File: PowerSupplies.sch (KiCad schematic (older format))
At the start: 37 parts, among them Q301 BC847B-13-F, Q302 BC856B-13-F, Q305 TK32A12N1,S4X, Q306 TK32A12N1,S4X, U301 FDA217, U302 LTC7138EMSE-PBF, U303 TPS560200, U304 TLV70430_SOT23-5

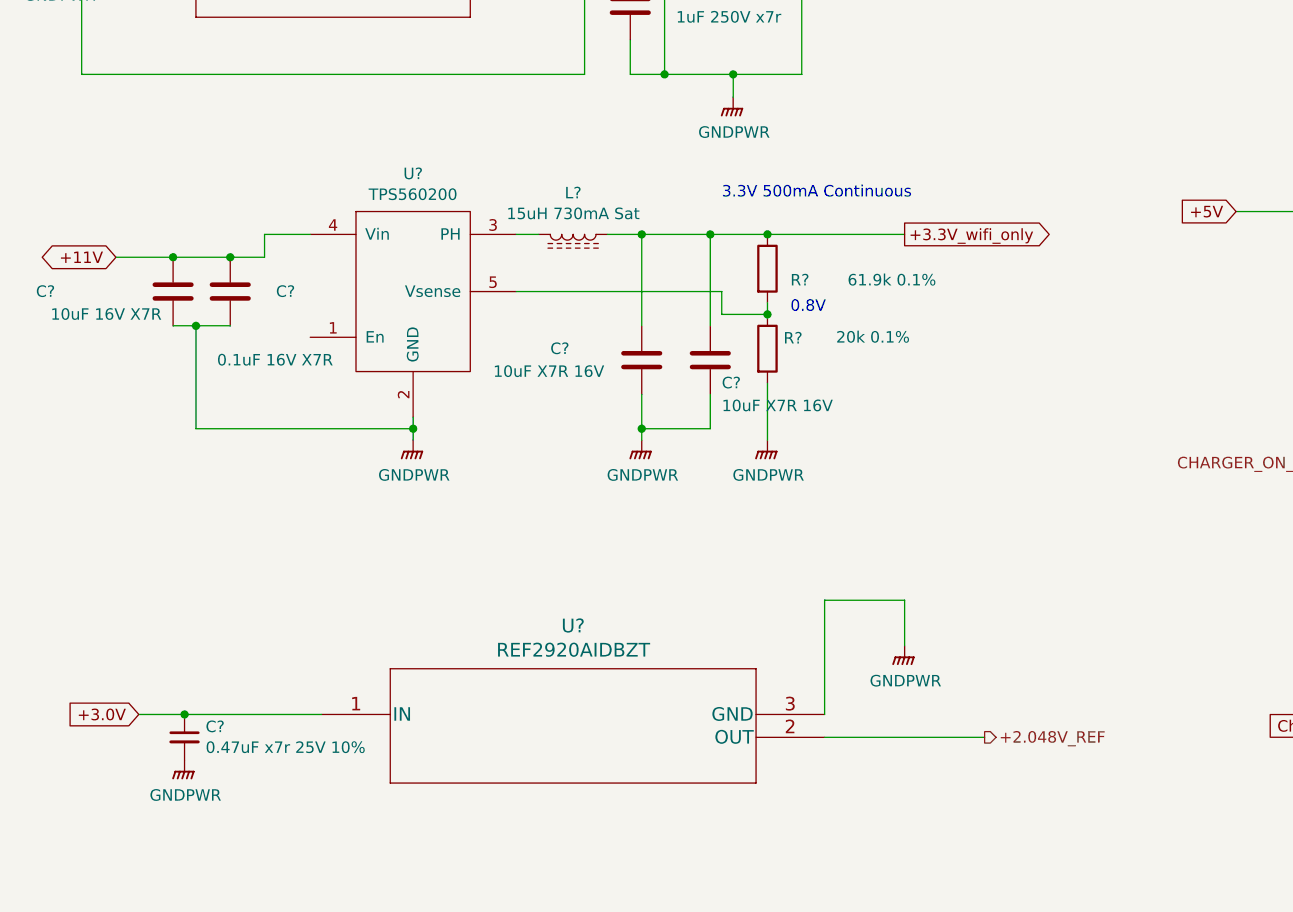
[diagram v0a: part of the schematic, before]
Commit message: started routing backing up tonnes of changes,2.048V reference changed to 2.5V ref, to match ucc2800, cos to change to a version with a 2V feedback, would require me to update the Oscillator cap and resistor,and also recalulate the class 2 loop compensation components etc.  Move the location of the teensy LC and added the ESP-WROOM-o2 wifi module.
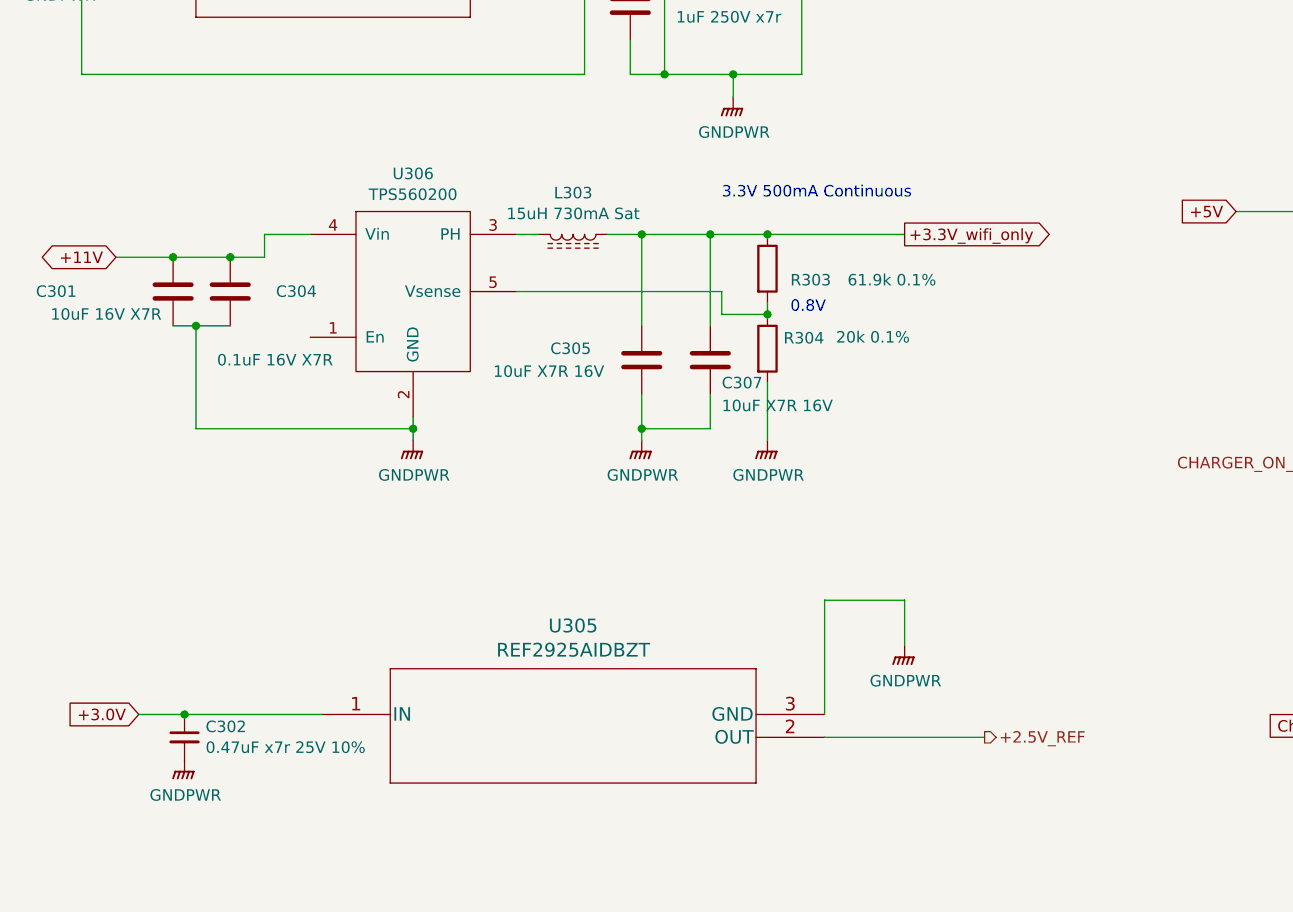
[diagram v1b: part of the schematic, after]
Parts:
- U305: renamed from U?; value REF2920AIDBZT -> REF2925AIDBZT
- gave numbers to parts that had none: 9
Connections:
- net +2.048V_REF renamed +2.5V_REF
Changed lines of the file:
@@
 5V 500mA Continuous
 Text HLabel 4750 5900 2    50   Output ~ 0
-+2.048V_REF
++2.5V_REF
 Text GLabel 950  3800 0    50   BiDi ~ 0
 +11V
@@
 P 2250 4600
 AR Path="/5F9C831E" Ref="#PWR?"  Part="1"
-AR Path="/5EBD6442/5F9C831E" Ref="#PWR?"  Part="1"
-F 0 "#PWR?" H 2250 4400 50  0001 C CNN
+AR Path="/5EBD6442/5F9C831E" Ref="#PWR0303"  Part="1"
+F 0 "#PWR0303" H 2250 4400 50  0001 C CNN
 F 1 "GNDPWR" H 2254 4446 50  0000 C CNN
 F 2 "" H 2250 4550 50  0001 C CNN
@@
 P 3550 4250
 AR Path="/5F9C8324" Ref="C?"  Part="1"
-AR Path="/5EBD6442/5F9C8324" Ref="C?"  Part="1"
-F 0 "C?" H 3600 4150 50  0000 L CNN
+AR Path="/5EBD6442/5F9C8324" Ref="C307"  Part="1"
+F 0 "C307" H 3600 4150 50  0000 L CNN
 F 1 "10uF X7R 16V" H 3600 4050 50  0000 L CNN
 F 2 "Capacitors_SMD:C_1206_HandSoldering" H 3588 4100 50  0001 C CNN
@@
 P 2950 3700
 AR Path="/5F9C832A" Ref="L?"  Part="1"
-AR Path="/5EBD6442/5F9C832A" Ref="L?"  Part="1"
-F 0 "L?" V 2769 3700 50  0000 C CNN
+AR Path="/5EBD6442/5F9C832A" Ref="L303"  Part="1"
+F 0 "L303" V 2769 3700 50  0000 C CNN
 F 1 "15uH 730mA Sat" V 2860 3700 50  0000 C CNN
 F 2 "Inductors_jl:Inductor_1210_HandSoldering" H 2950 3700 50  0001 C CNN
@@
 P 3250 4250
 AR Path="/5F9C8331" Ref="C?"  Part="1"
-AR Path="/5EBD6442/5F9C8331" Ref="C?"  Part="1"
-F 0 "C?" H 2850 4300 50  0000 L CNN
+AR Path="/5EBD6442/5F9C8331" Ref="C305"  Part="1"
+F 0 "C305" H 2850 4300 50  0000 L CNN
 F 1 "10uF X7R 16V" H 2600 4200 50  0000 L CNN
 F 2 "Capacitors_SMD:C_1206_HandSoldering" H 3288 4100 50  0001 C CNN
@@
 P 3800 3850
 AR Path="/5F9C8337" Ref="R?"  Part="1"
-AR Path="/5EBD6442/5F9C8337" Ref="R?"  Part="1"
-F 0 "R?" H 3900 3800 50  0000 L CNN
+AR Path="/5EBD6442/5F9C8337" Ref="R303"  Part="1"
+F 0 "R303" H 3900 3800 50  0000 L CNN
 F 1 "61.9k 0.1%" H 4150 3800 50  0000 L CNN
 F 2 "Resistors_SMD:R_0805_HandSoldering" V 3730 3850 50  0001 C CNN
@@
 P 3800 4200
 AR Path="/5F9C833D" Ref="R?"  Part="1"
-AR Path="/5EBD6442/5F9C833D" Ref="R?"  Part="1"
-F 0 "R?" H 3870 4246 50  0000 L CNN
+AR Path="/5EBD6442/5F9C833D" Ref="R304"  Part="1"
+F 0 "R304" H 3870 4246 50  0000 L CNN
 F 1 "20k 0.1%" H 4100 4250 50  0000 L CNN
 F 2 "Resistors_SMD:R_0805_HandSoldering" V 3730 4200 50  0001 C CNN
@@
 P 3800 4600
 AR Path="/5F9C8343" Ref="#PWR?"  Part="1"
-AR Path="/5EBD6442/5F9C8343" Ref="#PWR?"  Part="1"
-F 0 "#PWR?" H 3800 4400 50  0001 C CNN
+AR Path="/5EBD6442/5F9C8343" Ref="#PWR0305"  Part="1"
+F 0 "#PWR0305" H 3800 4400 50  0001 C CNN
 F 1 "GNDPWR" H 3804 4446 50  0000 C CNN
 F 2 "" H 3800 4550 50  0001 C CNN
@@
 P 3250 4600
 AR Path="/5F9C834D" Ref="#PWR?"  Part="1"
-AR Path="/5EBD6442/5F9C834D" Ref="#PWR?"  Part="1"
-F 0 "#PWR?" H 3250 4400 50  0001 C CNN
+AR Path="/5EBD6442/5F9C834D" Ref="#PWR0304"  Part="1"
+F 0 "#PWR0304" H 3250 4400 50  0001 C CNN
 F 1 "GNDPWR" H 3254 4446 50  0000 C CNN
 F 2 "" H 3250 4550 50  0001 C CNN
@@
 P 1200 3950
 AR Path="/5F9C8354" Ref="C?"  Part="1"
-AR Path="/5EBD6442/5F9C8354" Ref="C?"  Part="1"
-F 0 "C?" H 600 3950 50  0000 L CNN
+AR Path="/5EBD6442/5F9C8354" Ref="C301"  Part="1"
+F 0 "C301" H 600 3950 50  0000 L CNN
 F 1 "10uF 16V X7R" H 1150 3850 50  0000 R CNN
 F 2 "Capacitors_SMD:C_1206_HandSoldering" H 1238 3800 50  0001 C CNN
@@
 0.8V
 $Comp
-L TI:TPS560200 U?
+L TI:TPS560200 U306
 U 1 1 5F9C8360
 P 2250 3950
-F 0 "U?" H 2250 4465 50  0000 C CNN
+F 0 "U306" H 2250 4465 50  0000 C CNN
 F 1 "TPS560200" H 2250 4374 50  0000 C CNN
 F 2 "Package_TO_SOT_SMD:SOT-23-5_HandSoldering" H 2250 3950 50  0001 C CNN
@@
 P 1450 3950
 AR Path="/5F9C836F" Ref="C?"  Part="1"
-AR Path="/5EBD6442/5F9C836F" Ref="C?"  Part="1"
-F 0 "C?" H 1650 3950 50  0000 L CNN
+AR Path="/5EBD6442/5F9C836F" Ref="C304"  Part="1"
+F 0 "C304" H 1650 3950 50  0000 L CNN
 F 1 "0.1uF 16V X7R" H 1900 3650 50  0000 R CNN
 F 2 "Capacitors_SMD:C_0805_HandSoldering" H 1488 3800 50  0001 C CNN
@@
 3.3V 500mA Continuous
 $Comp
-L TI:REF2920AIDBZT U?
+L TI:REF2920AIDBZT U305
 U 1 1 5FB58010
 P 1850 5800
-F 0 "U?" H 2950 6187 60  0000 C CNN
-F 1 "REF2920AIDBZT" H 2950 6081 60  0000 C CNN
+F 0 "U305" H 2950 6187 60  0000 C CNN
+F 1 "REF2925AIDBZT" H 2950 6081 60  0000 C CNN
 F 2 "Package_TO_SOT_SMD:SOT-23_Handsoldering" H 2950 6040 60  0001 C CNN
 F 3 "" H 1850 5800 60  0000 C CNN
@@
 P 4400 5500
 AR Path="/5FB595B9" Ref="#PWR?"  Part="1"
-AR Path="/5EBD6442/5FB595B9" Ref="#PWR?"  Part="1"
-F 0 "#PWR?" H 4400 5300 50  0001 C CNN
+AR Path="/5EBD6442/5FB595B9" Ref="#PWR0306"  Part="1"
+F 0 "#PWR0306" H 4400 5300 50  0001 C CNN
 F 1 "GNDPWR" H 4404 5346 50  0000 C CNN
 F 2 "" H 4400 5450 50  0001 C CNN
@@
 	4050 5900 4750 5900
 $Comp
-L Device:C_Small C?
+L Device:C_Small C302
 U 1 1 5FB88319
 P 1250 5900
-F 0 "C?" H 1342 5946 50  0000 L CNN
+F 0 "C302" H 1342 5946 50  0000 L CNN
 F 1 "0.47uF x7r 25V 10%" H 1342 5855 50  0000 L CNN
 F 2 "Capacitors_SMD:C_0805_HandSoldering" H 1250 5900 50  0001 C CNN
@@
 P 1250 6000
 AR Path="/5FB8F7FD" Ref="#PWR?"  Part="1"
-AR Path="/5EBD6442/5FB8F7FD" Ref="#PWR?"  Part="1"
-F 0 "#PWR?" H 1250 5800 50  0001 C CNN
+AR Path="/5EBD6442/5FB8F7FD" Ref="#PWR0302"  Part="1"
+F 0 "#PWR0302" H 1250 5800 50  0001 C CNN
 F 1 "GNDPWR" H 1254 5846 50  0000 C CNN
 F 2 "" H 1250 5950 50  0001 C CNN

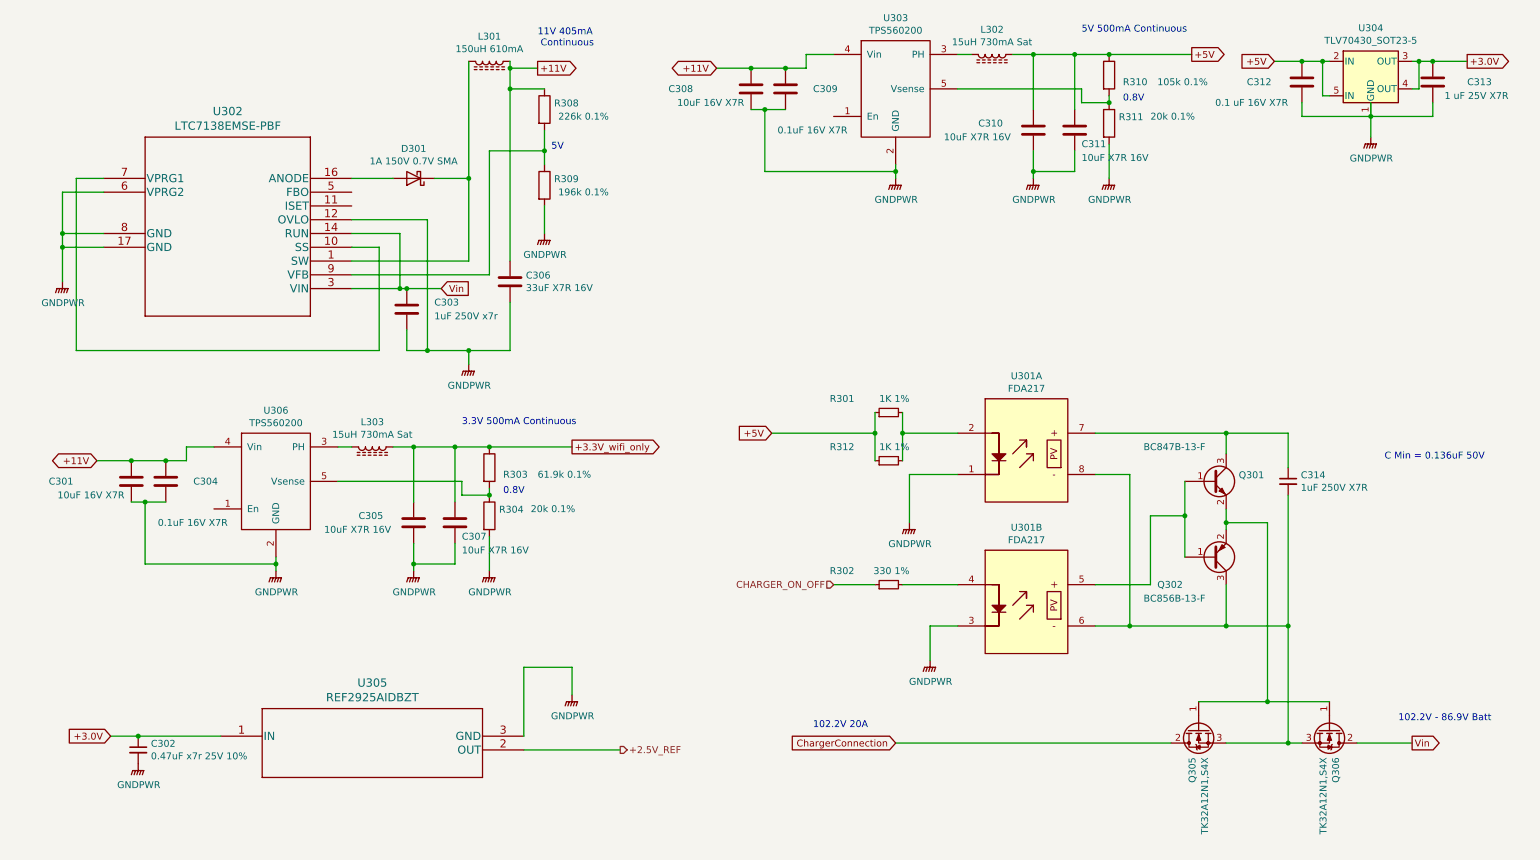
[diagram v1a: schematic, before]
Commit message: added testpoints
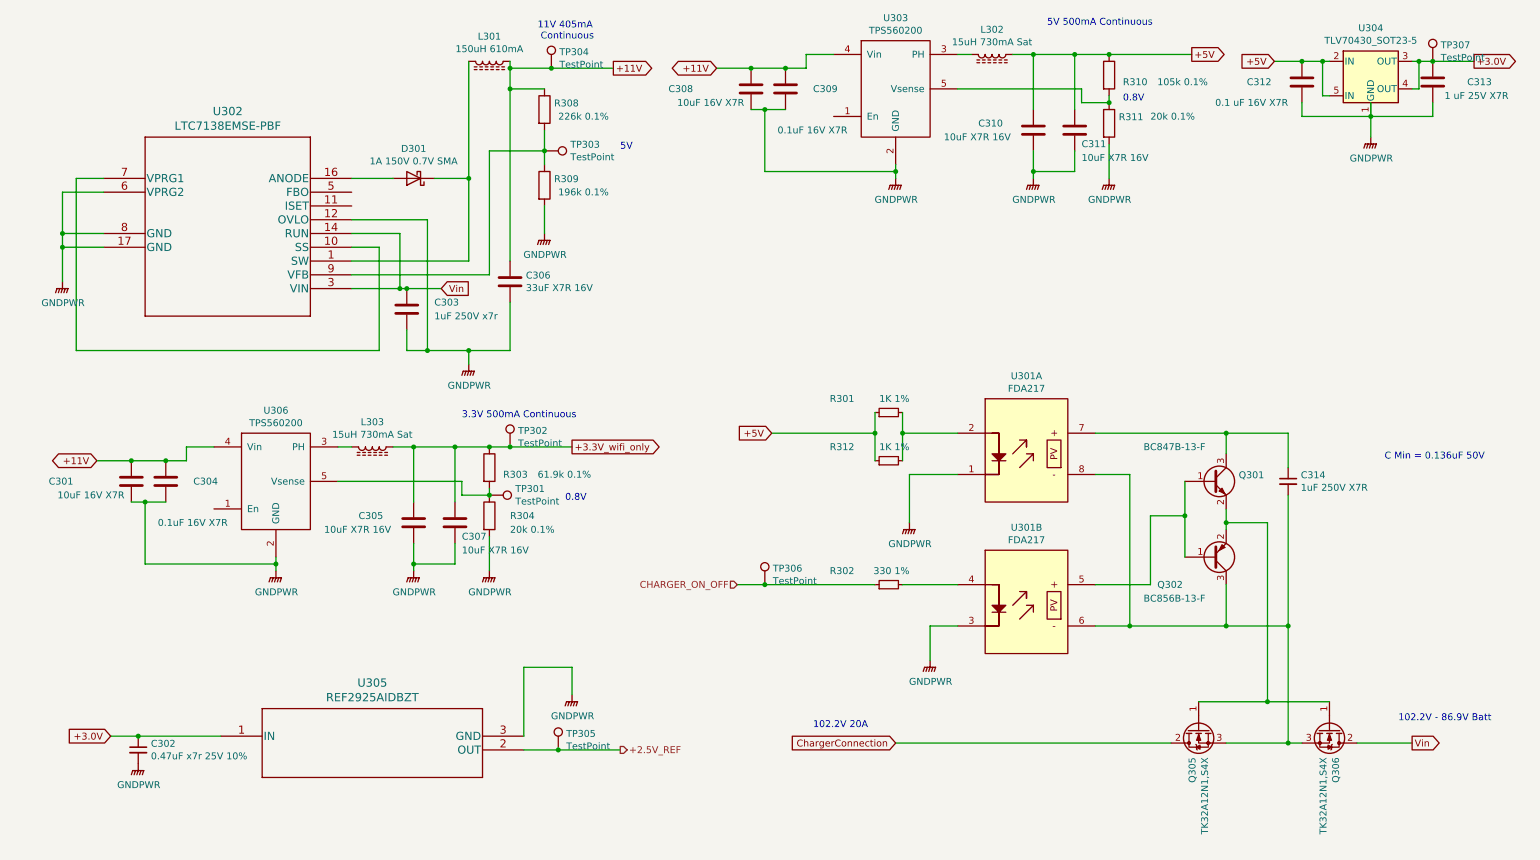
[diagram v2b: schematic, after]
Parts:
- added TP301, TP302, TP303, TP304, TP305, TP306, TP307: TestPoint, Measurement_Points:Measurement_Point_Square-SMD-Pad_Big, symbol Connector:TestPoint
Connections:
- net +11V: now also TP304.1
- net +2.5V_REF: now also TP305.1
- net +3.0V: now also TP307.1
- net +3.3V_wifi_only: now also TP302.1
- net CHARGER_ON_OFF: now also TP306.1
- net at R308.2, R309.1, U302.9 (VFB): now also TP303.1
- net at R303.2, R304.1, U306.5 (Vsense): now also TP301.1
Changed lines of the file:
@@
 Wire Wire Line
 	3650 1750 3650 900
-Text GLabel 4150 950  2    50   Output ~ 0
+Text GLabel 4700 950  2    50   Output ~ 0
 +11V
 Wire Wire Line
-	4150 950  3950 950
+	4700 950  4250 950
 Wire Wire Line
 	3950 900  3950 950
@@
 Wire Wire Line
 	2800 1750 3100 1750
-Text Notes 4250 1550 0    50   ~ 0
+Text Notes 4750 1550 0    50   ~ 0
 5V
 Wire Wire Line
@@
 Wire Wire Line
 	8300 1750 8300 1500
-Wire Wire Line
-	8300 850  8900 850
 Connection ~ 8300 850
 $Comp
@@
 	9500 900  9700 900
 Connection ~ 9700 900
-Text GLabel 10900 900  2    50   Output ~ 0
+Text GLabel 10950 900  2    50   Output ~ 0
 +3.0V
-Wire Wire Line
-	10900 900  10650 900
 Connection ~ 10650 900
 $Comp
@@
 Text Notes 6150 5750 0    50   ~ 0
 102.2V 20A
-Text HLabel 6300 4700 0    50   Input ~ 0
+Text HLabel 5600 4700 0    50   Input ~ 0
 CHARGER_ON_OFF
 $Comp
@@
 	6800 4700 7200 4700
 Wire Wire Line
-	6600 4700 6300 4700
+	6600 4700 5800 4700
 $Comp
 L Device:R_Small R301
@@
 Wire Wire Line
 	9850 900  9900 900
-Text Notes 4150 800  0    50   ~ 0
+Text Notes 4150 750  0    50   ~ 0
 11V 405mA\n Continuous
-Text Notes 8100 700  0    50   ~ 0
+Text Notes 7850 650  0    50   ~ 0
 5V 500mA Continuous
 Text HLabel 4750 5900 2    50   Output ~ 0
@@
 AR Path="/5F9C833D" Ref="R?"  Part="1"
 AR Path="/5EBD6442/5F9C833D" Ref="R304"  Part="1"
-F 0 "R304" H 3870 4246 50  0000 L CNN
-F 1 "20k 0.1%" H 4100 4250 50  0000 L CNN
+F 0 "R304" H 3950 4200 50  0000 L CNN
+F 1 "20k 0.1%" H 3950 4100 50  0000 L CNN
 F 2 "Resistors_SMD:R_0805_HandSoldering" V 3730 4200 50  0001 C CNN
 F 3 "~" H 3800 4200 50  0001 C CNN
@@
 Wire Wire Line
 	2250 4550 2250 4600
-Text Notes 3900 4050 0    50   ~ 0
+Text Notes 4350 4100 0    50   ~ 0
 0.8V
 $Comp
@@
 Wire Wire Line
 	3800 4600 3800 4350
-Wire Wire Line
-	3800 3700 4400 3700
 Connection ~ 3800 3700
-Text Notes 3600 3550 0    50   ~ 0
+Text Notes 3600 3500 0    50   ~ 0
 3.3V 500mA Continuous
 $Comp
@@
 +3.0V
 Wire Wire Line
-	4050 5900 4750 5900
+	4050 5900 4300 5900
 $Comp
 L Device:C_Small C302
@@
 	1250 5800 1850 5800
 Connection ~ 1250 5800
+$Comp
+L Connector:TestPoint TP304
+U 1 1 60423F90
+P 4250 950
+F 0 "TP304" H 4308 1068 50  0000 L CNN
+F 1 "TestPoint" H 4308 977 50  0000 L CNN
+F 2 "Measurement_Points:Measurement_Point_Square-SMD-Pad_Big" H 4450 950 50  0001 C CNN
+F 3 "~" H 4450 950 50  0001 C CNN
+	1    4250 950
+	1    0    0    -1
+$EndComp
+Connection ~ 4250 950
+Wire Wire Line
+	4250 950  3950 950
+$Comp
+L Connector:TestPoint TP303
+U 1 1 6045A6ED
+P 4200 1550
+F 0 "TP303" V 4154 1738 50  0000 L CNN
+F 1 "TestPoint" V 4245 1738 50  0000 L CNN
+F 2 "Measurement_Points:Measurement_Point_Square-SMD-Pad_Big" H 4400 1550 50  0001 C CNN
+F 3 "~" H 4400 1550 50  0001 C CNN
+	1    4200 1550
+	0    1    1    0
+$EndComp
+$Comp
+L Connector:TestPoint TP301
+U 1 1 60490DE8
+P 3800 4050
+F 0 "TP301" V 3754 4238 50  0000 L CNN
+F 1 "TestPoint" V 3845 4238 50  0000 L CNN
+F 2 "Measurement_Points:Measurement_Point_Square-SMD-Pad_Big" H 4000 4050 50  0001 C CNN
+F 3 "~" H 4000 4050 50  0001 C CNN
+	1    3800 4050
+	0    1    1    0
+$EndComp
+$Comp
+L Connector:TestPoint TP305
+U 1 1 60497068
+P 4300 5900
+F 0 "TP305" H 4358 6018 50  0000 L CNN
+F 1 "TestPoint" H 4358 5927 50  0000 L CNN
+F 2 "Measurement_Points:Measurement_Point_Square-SMD-Pad_Big" H 4500 5900 50  0001 C CNN
+F 3 "~" H 4500 5900 50  0001 C CNN
+	1    4300 5900
+	1    0    0    -1
+$EndComp
+Connection ~ 4300 5900
+Wire Wire Line
+	4300 5900 4750 5900
+Wire Wire Line
+	8300 850  8900 850
+Wire Wire Line
+	3800 3700 3950 3700
+$Comp
+L Connector:TestPoint TP307
+U 1 1 6049E6F4
+P 10650 900
+F 0 "TP307" H 10708 1018 50  0000 L CNN
+F 1 "TestPoint" H 10708 927 50  0000 L CNN
+F 2 "Measurement_Points:Measurement_Point_Square-SMD-Pad_Big" H 10850 900 50  0001 C CNN
+F 3 "~" H 10850 900 50  0001 C CNN
+	1    10650 900
+	1    0    0    -1
+$EndComp
+$Comp
+L Connector:TestPoint TP302
+U 1 1 6049EF33
+P 3950 3700
+F 0 "TP302" H 4008 3818 50  0000 L CNN
+F 1 "TestPoint" H 4008 3727 50  0000 L CNN
+F 2 "Measurement_Points:Measurement_Point_Square-SMD-Pad_Big" H 4150 3700 50  0001 C CNN
+F 3 "~" H 4150 3700 50  0001 C CNN
+	1    3950 3700
+	1    0    0    -1
+$EndComp
+Connection ~ 3950 3700
+Wire Wire Line
+	3950 3700 4400 3700
+$Comp
+L Connector:TestPoint TP306
+U 1 1 604A0C2F
+P 5800 4700
+F 0 "TP306" H 5858 4818 50  0000 L CNN
+F 1 "TestPoint" H 5858 4727 50  0000 L CNN
+F 2 "Measurement_Points:Measurement_Point_Square-SMD-Pad_Big" H 6000 4700 50  0001 C CNN
+F 3 "~" H 6000 4700 50  0001 C CNN
+	1    5800 4700
+	1    0    0    -1
+$EndComp
+Wire Wire Line
+	10650 900  10950 900
+Connection ~ 5800 4700
+Wire Wire Line
+	5800 4700 5600 4700
 $EndSCHEMATC
